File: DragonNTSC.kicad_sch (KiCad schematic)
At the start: 19 parts, among them IC1 74LS273N, IC2 MC6847, IC3 MC1372, J1 Board interconnect, J2 Video Output, Q161 2N4403, Q162 2N4401

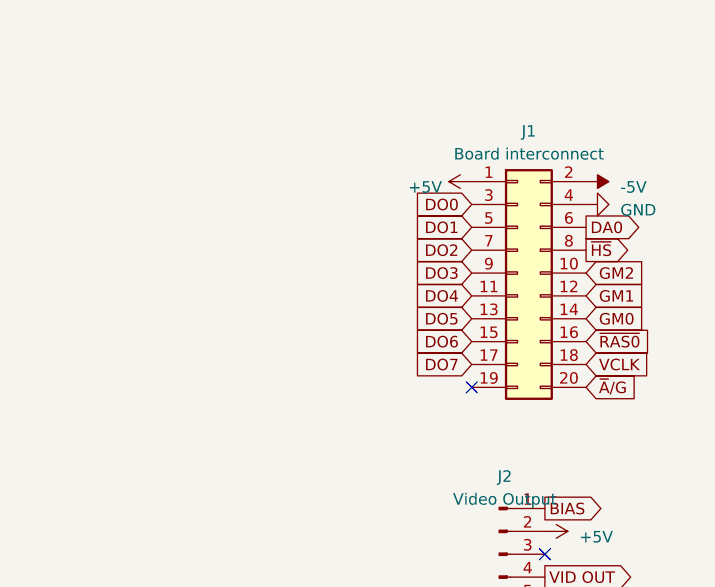
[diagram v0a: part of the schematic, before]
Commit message: add missing css and fs lines
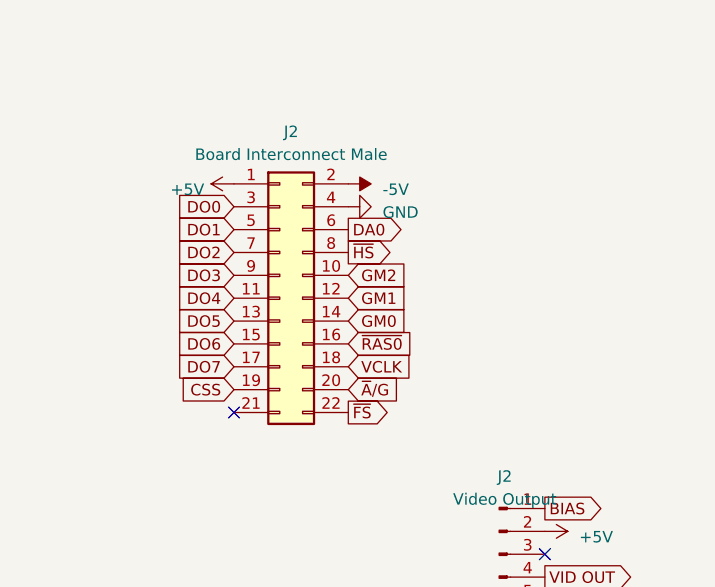
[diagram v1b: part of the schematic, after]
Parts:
- removed J1: Board interconnect, Connector_PinHeader_2.54mm:PinHeader_2x10_P2.54mm_Vertical, symbol Connector_Generic:Conn_02x10_Odd_Even
- added J2: Board Interconnect Male, Connector_PinHeader_2.54mm:PinHeader_2x11_P2.54mm_Vertical, symbol Connector_Generic:Conn_02x11_Odd_Even
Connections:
- net +5V: now also J2.1 (Pin_1)
- net -5V: now also J2.2 (Pin_2)
- net CSS: now also J2.19 (Pin_19)
- net DA0: now also J2.6 (Pin_6)
- net DO0: now also J2.3 (Pin_3)
- net DO1: now also J2.5 (Pin_5)
- net DO2: now also J2.7 (Pin_7)
- net DO3: now also J2.9 (Pin_9)
- net DO4: now also J2.11 (Pin_11)
- net DO5: now also J2.13 (Pin_13)
- net DO6: now also J2.15 (Pin_15)
- net DO7: now also J2.17 (Pin_17)
- net GM0: now also J2.14 (Pin_14)
- net GM1: now also J2.12 (Pin_12)
- net GM2: now also J2.10 (Pin_10)
- net GND: now also J2.4 (Pin_4)
- net VCLK: now also J2.18 (Pin_18)
- net ~{A}/G: now also J2.20 (Pin_20)
- net ~{FS}: now also J2.22 (Pin_22)
- net ~{HS}: now also J2.8 (Pin_8)
- net ~{RAS0}: now also J2.16 (Pin_16)

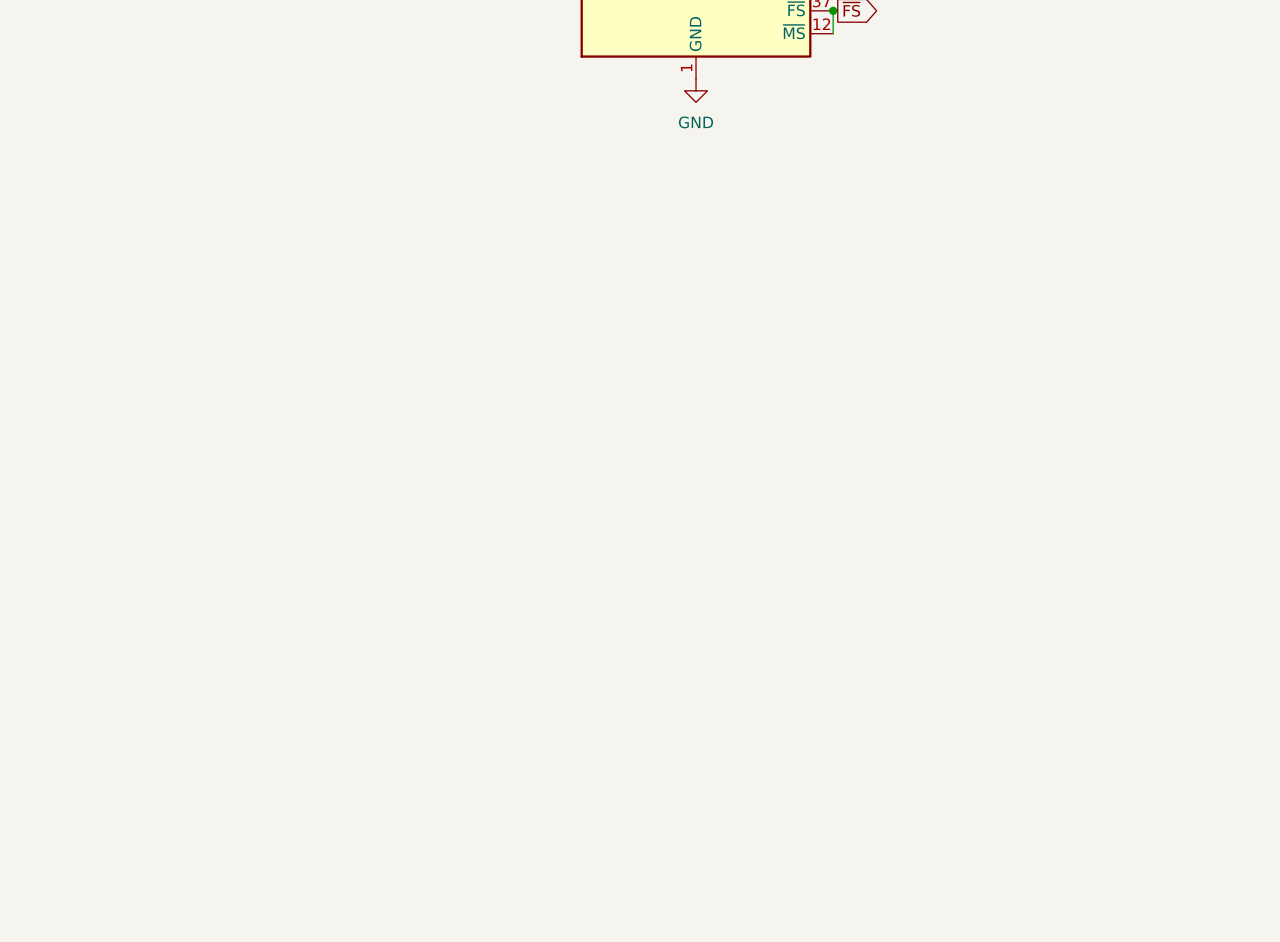
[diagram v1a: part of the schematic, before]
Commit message: add 555 timer
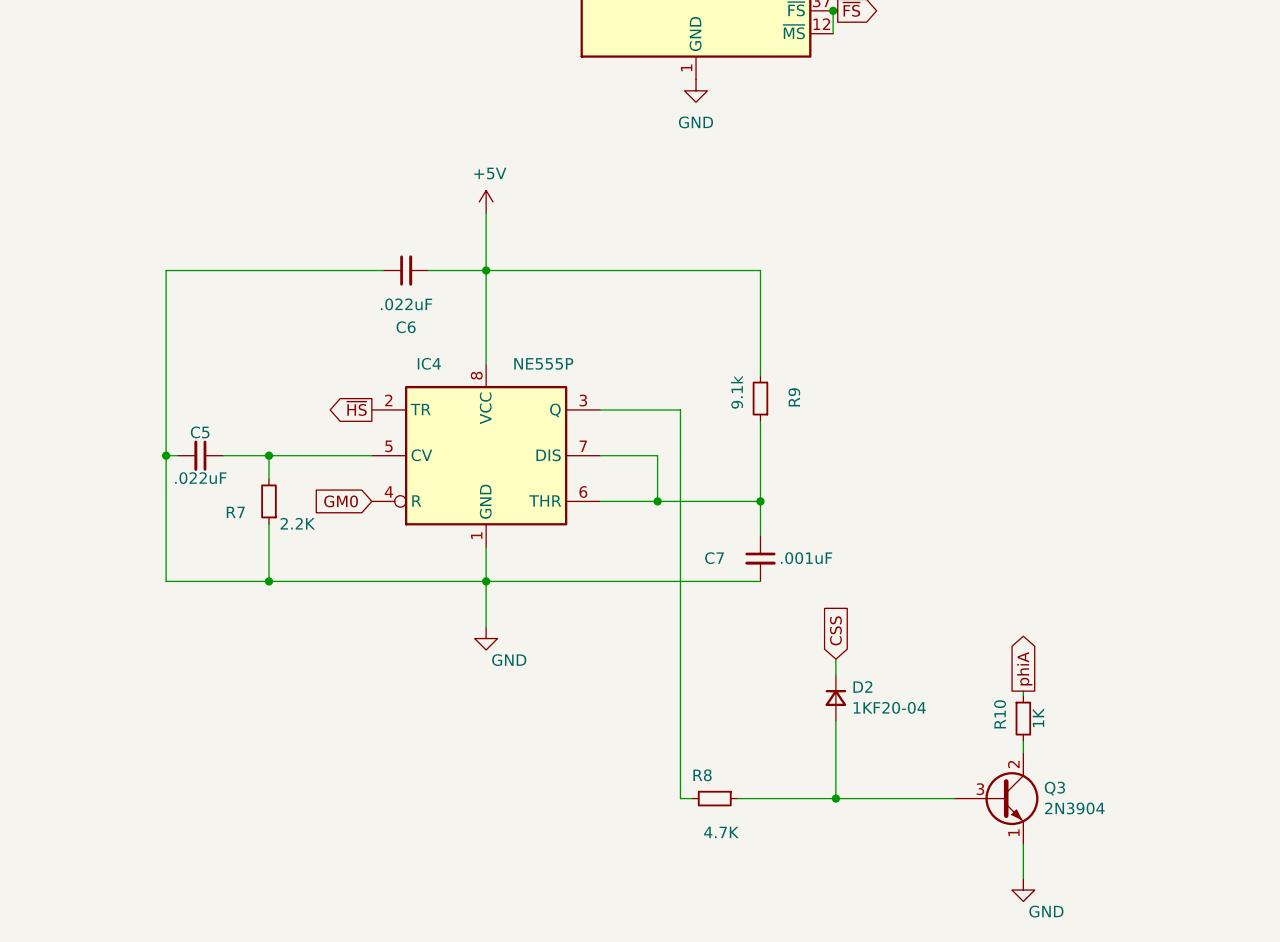
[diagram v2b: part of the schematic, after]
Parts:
- added C5, C6: .022uF, Capacitor_THT:C_Disc_D8.0mm_W2.5mm_P5.00mm, symbol Device:C_Small
- added C7: .001uF, Capacitor_THT:C_Rect_L4.0mm_W2.5mm_P2.50mm, symbol Device:C_Small
- added D2: 1KF20-04, Diode_THT:D_A-405_P10.16mm_Horizontal, symbol Device:D_Small
- added IC4: NE555P, Package_DIP:DIP-8_W7.62mm, symbol Timer:NE555P
- added Q3: 2N3904, Package_TO_SOT_THT:TO-92_Inline, symbol Device:Q_NPN_ECB
- added R10: 1K, Resistor_THT:R_Axial_DIN0207_L6.3mm_D2.5mm_P2.54mm_Vertical, symbol Device:R_Small
- added R7: 2.2K, Resistor_THT:R_Axial_DIN0207_L6.3mm_D2.5mm_P2.54mm_Vertical, symbol Device:R_Small
- added R8: 4.7K, Resistor_THT:R_Axial_DIN0207_L6.3mm_D2.5mm_P2.54mm_Vertical, symbol Device:R_Small
- added R9: 9.1k, Resistor_THT:R_Axial_DIN0207_L6.3mm_D2.5mm_P2.54mm_Vertical, symbol Device:R_Small
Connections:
- net +5V: now also C6.2, IC4.8 (VCC), R9.2
- net CSS: now also D2.1 (K)
- net GM0: now also IC4.4 (R)
- net GND: now also C5.2, C6.1, C7.2, IC4.1 (GND), Q3.1 (E), R7.1
- net phiA: now also R10.1
- net ~{HS}: now also IC4.2 (TR)
- new net: Q3.2 (C), R10.2
- new net: D2.2 (A), Q3.3 (B), R8.1
- new net: C7.1, IC4.6 (THR), IC4.7 (DIS), R9.1
- new net: IC4.3 (Q), R8.2
- new net: C5.1, IC4.5 (CV), R7.2

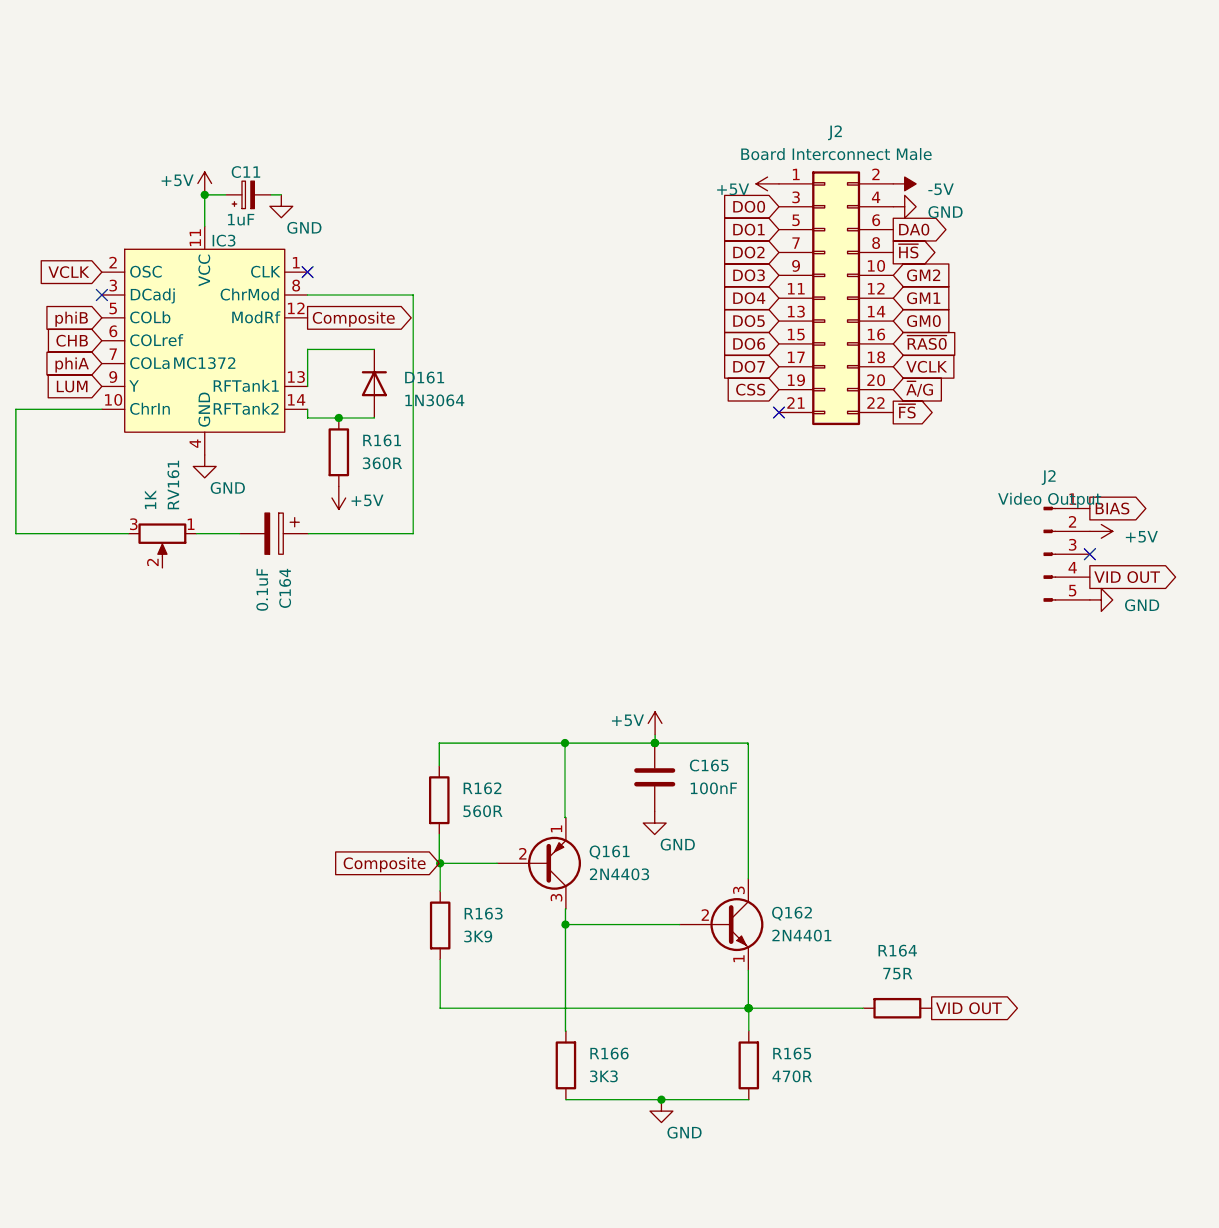
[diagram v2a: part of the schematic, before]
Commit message: migrate to kicad 9
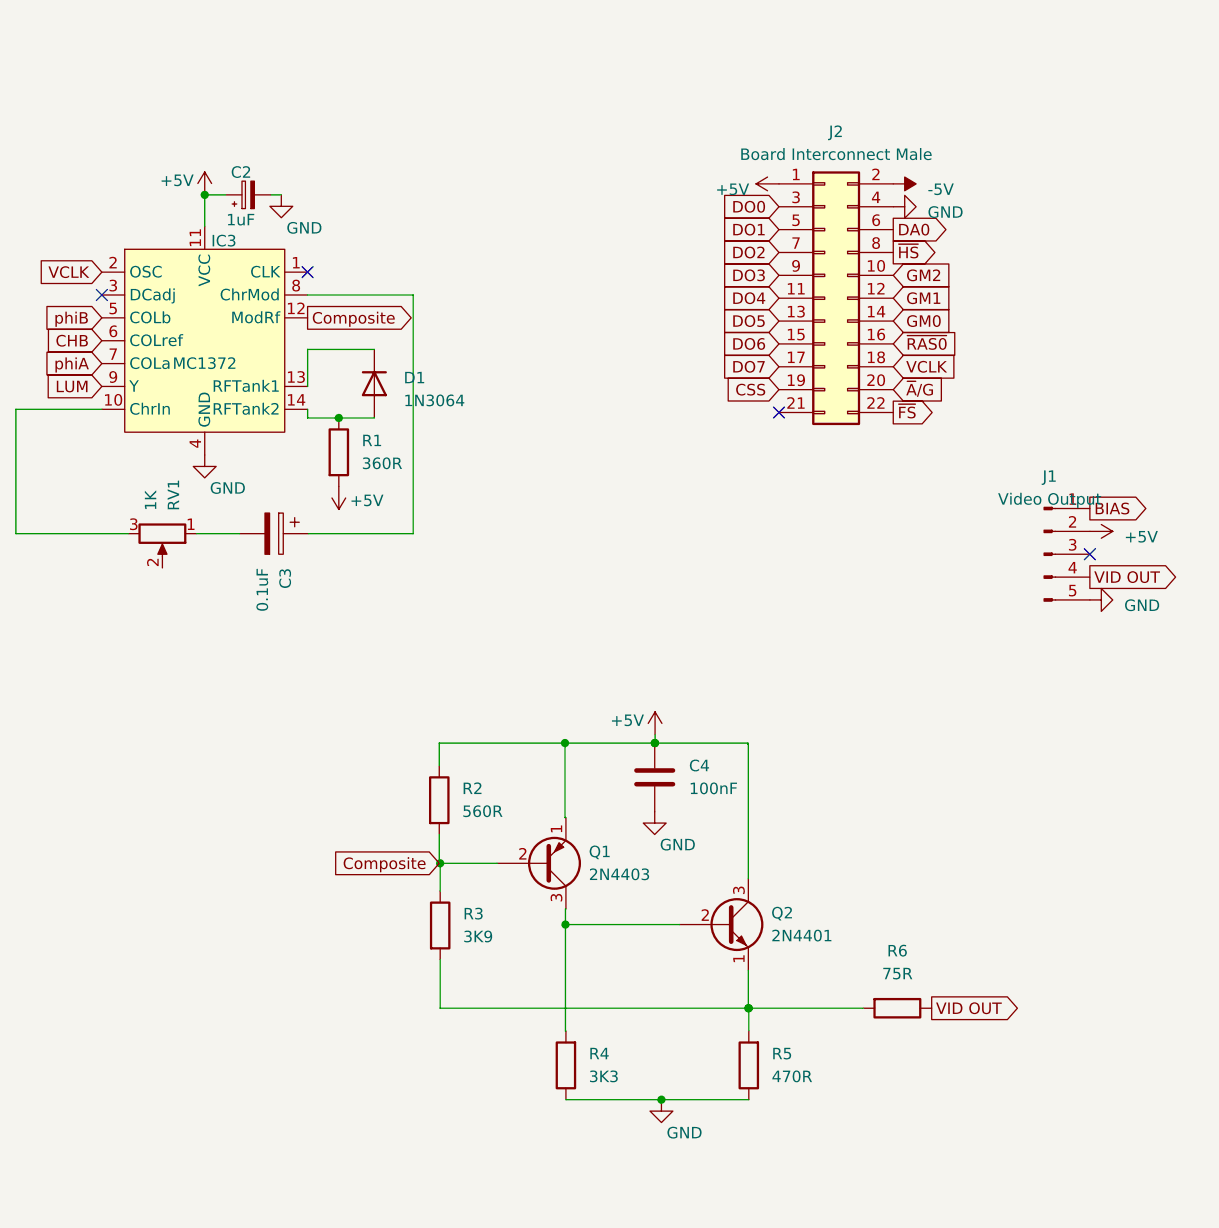
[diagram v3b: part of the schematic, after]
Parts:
- renumbered C11 to C2, C164 to C3, C165 to C4, D161 to D1, J2 to J1, Q161 to Q1, Q162 to Q2, R161 to R1, R162 to R2, R163 to R3, R166 to R4, R165 to R5, R164 to R6, RV161 to RV1

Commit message: revise for fab
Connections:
- net -5V: now also J1.3 (Pin_3); no longer J2.2 (Pin_2)
- net at C3.2: now also RV1.2; no longer RV1.1
- no-connect marks 17 -> 18
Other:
- moved on the sheet: C2, C3, D1, IC3, R1, RV1
